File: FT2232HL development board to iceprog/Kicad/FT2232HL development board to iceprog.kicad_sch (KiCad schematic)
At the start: 4 parts, among them J1 Conn_02x05_Odd_Even, P1 Conn_01x19_Male, P2 Conn_01x19_Male

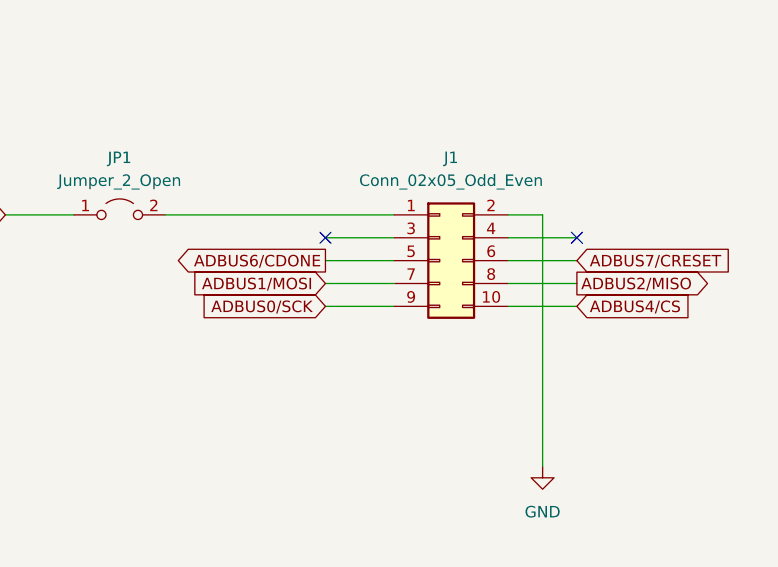
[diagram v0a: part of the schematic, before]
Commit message: Swapped MOSI/MISO.
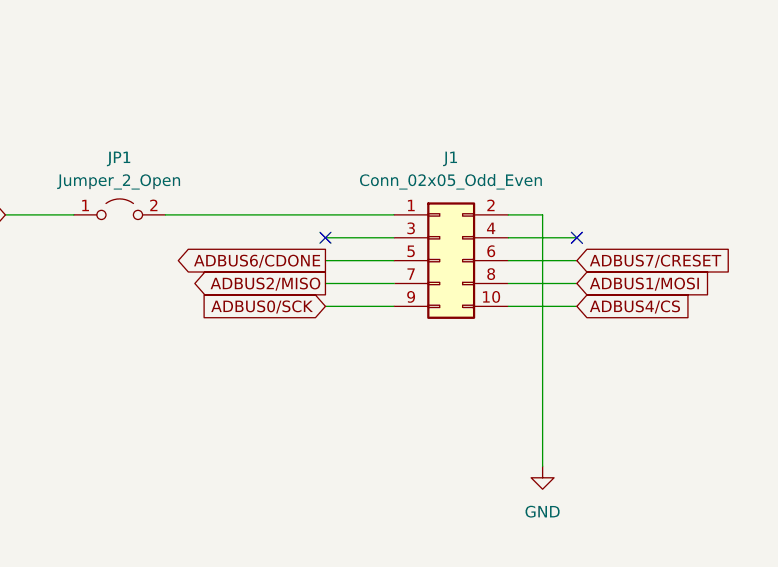
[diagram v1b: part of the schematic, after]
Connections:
- net ADBUS1/MOSI: now also J1.8 (Pin_8); no longer J1.7 (Pin_7)
- net ADBUS2/MISO: now also J1.7 (Pin_7); no longer J1.8 (Pin_8)
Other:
- company: (none) -> https://github.com/atoomnetmarc/FT2232HL-development-board-adapters
- title: (none) -> FT2232HL development board to iceprog
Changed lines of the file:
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@@
 (kicad_sch (version 20211123) (generator eeschema)
   (paper "A4")
+  (title_block
+    (title "FT2232HL development board to iceprog")
+    (date "2022-12-20")
+    (rev "1")
+    (company "https://github.com/atoomnetmarc/FT2232HL-development-board-adapters")
+  )
   (junction (at 77.47 35.56) (diameter 0) (color 0 0 0 0)
   )
@@
     )
   )
-  (global_label "ADBUS1{slash}MOSI" (shape input) (at 193.04 59.69 180) (fields_autoplaced)
-    (effects (font (size 1.27 1.27)) (justify right))
-    (property "Intersheet References" "${INTERSHEET_REFS}" (id 0) (at 177.3221 59.6106 0)
-      (effects (font (size 1.27 1.27)) (justify right) hide)
+  (global_label "ADBUS1{slash}MOSI" (shape input) (at 220.98 59.69 0) (fields_autoplaced)
+    (effects (font (size 1.27 1.27)) (justify left))
+    (property "Intersheet References" "${INTERSHEET_REFS}" (id 0) (at 236.6979 59.7694 0)
+      (effects (font (size 1.27 1.27)) (justify left) hide)
     )
   )
@@
     )
   )
-  (global_label "ADBUS2{slash}MISO" (shape output) (at 220.98 59.69 0) (fields_autoplaced)
-    (effects (font (size 1.27 1.27)) (justify left))
-    (property "Intersheet References" "${INTERSHEET_REFS}" (id 0) (at 236.6979 59.6106 0)
-      (effects (font (size 1.27 1.27)) (justify left) hide)
+  (global_label "ADBUS2{slash}MISO" (shape output) (at 193.04 59.69 180) (fields_autoplaced)
+    (effects (font (size 1.27 1.27)) (justify right))
+    (property "Intersheet References" "${INTERSHEET_REFS}" (id 0) (at 177.3221 59.7694 0)
+      (effects (font (size 1.27 1.27)) (justify right) hide)
     )
   )
